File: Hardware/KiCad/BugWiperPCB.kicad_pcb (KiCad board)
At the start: 4 copper layers, 110 x 40 mm, 105 parts, among them J1 UJ20-C-H-G-SMT-1-P16-TR, J2 1770924, J3 Phoenix_1776508, J4 RJ45, J5 Conn_TagConnect_TC2030-NL_ESP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, J6 1824420000, J7 Conn_01x02_Pin, Q1 NMOS_SO-8, U1 ESP32-S3-WROOM-1, U2 BTN9960LV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

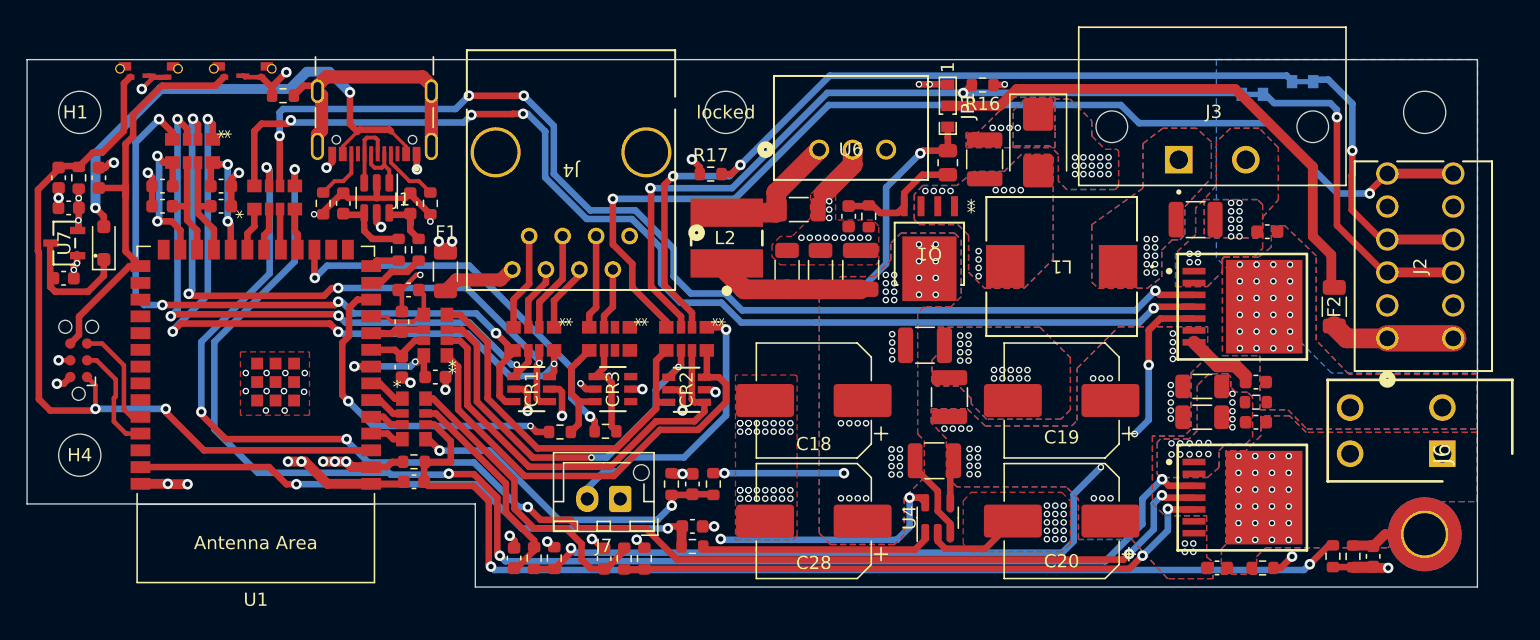
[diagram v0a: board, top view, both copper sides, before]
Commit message: update PCB
Add voltage selector solder jumper vor rj45 connector to switch between 12V and 3.3V vor the control panel
Add voltage supression diodes for IS pins from the motor driver ICs
Fix DRC violations
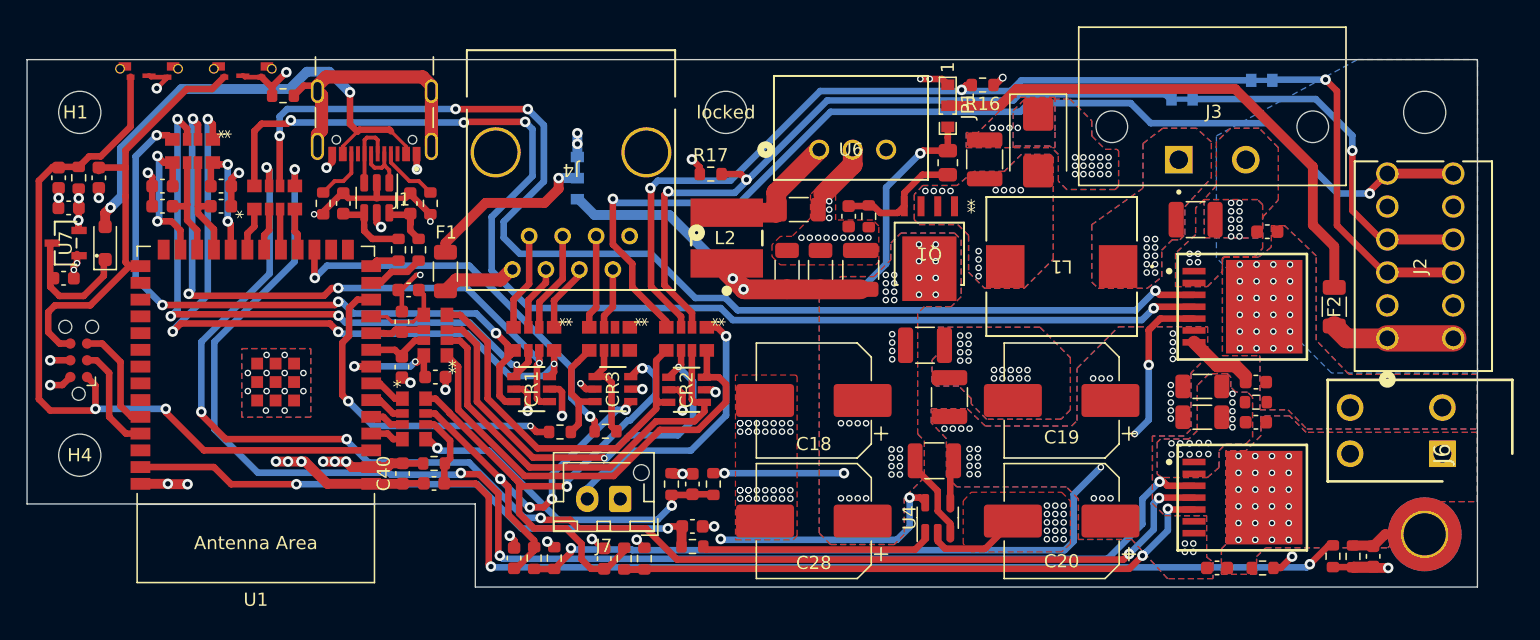
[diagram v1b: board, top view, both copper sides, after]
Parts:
- added C40: 1uF, Capacitor_SMD:C_0603_1608Metric, F.Cu at (138.5, 91.4)
- added JP4: SolderJumper_3_Bridged12, BugWiper_lib:SolderJumper_3P_R_SMD_0603_Bridged_12, B.Cu at (151.7, 69.0)
- moved JP2 9.24 mm to (196.8, 63.0)
- moved R38 1.53 mm to (140.9, 90.6)
- moved C31 1.53 mm to (140.9, 92.1)
- moved JP3 1.28 mm to (202.8, 61.6)
- moved D1 0.10 mm to (115.9, 73.9)
- moved U7 0.10 mm to (112.9, 73.9)
- turned C3 to -90 degrees
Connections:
- CR3 pad 4: unconnected-(CR3-IO_3-Pad4) -> /ESP32-S3/M_IS2
- CR3 pad 6: unconnected-(CR3-IO_4-Pad6) -> /ESP32-S3/M_IS1
- F1 pad 1: +3.3V -> Net-(JP4-C)
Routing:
- net /ESP32-S3/M_IS1: track 23.2 -> 40.9 mm, vias 0 -> 2
- net +12V: track 43.8 -> 59.2 mm, vias 39 -> 41
- net /ESP32-S3/M_IS2: track 16.4 -> 31.7 mm, vias 0 -> 4
- net Net-(JP4-C): track 0.00 -> 13.3 mm, vias 0 -> 1
- net Enc_1: track 64.4 -> 54.9 mm
- net EN_C1: track 20.3 -> 27.5 mm
- net /ESP32-S3/M_IHN2: track 87.1 -> 93.1 mm
- net /ESP32-S3/M_IN2: track 86.3 -> 91.2 mm
- net /ESP32-S3/ADC_NTC: track 82.8 -> 79.6 mm
- net Net-(CR2-IO_1): track 30.2 -> 33.3 mm
- net Net-(CR1-IO_2): track 52.6 -> 49.8 mm
- net +3.3V: track 39.7 -> 41.8 mm
- net GND: track 88.0 -> 89.5 mm, vias 170 -> 173
- net Net-(D1-A): track 38.2 -> 36.7 mm
- net Enc_2: track 60.1 -> 61.3 mm
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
